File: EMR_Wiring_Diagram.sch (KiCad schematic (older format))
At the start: 22 parts, among them SW1 Switch_DPST, SW2 Switch_DPST

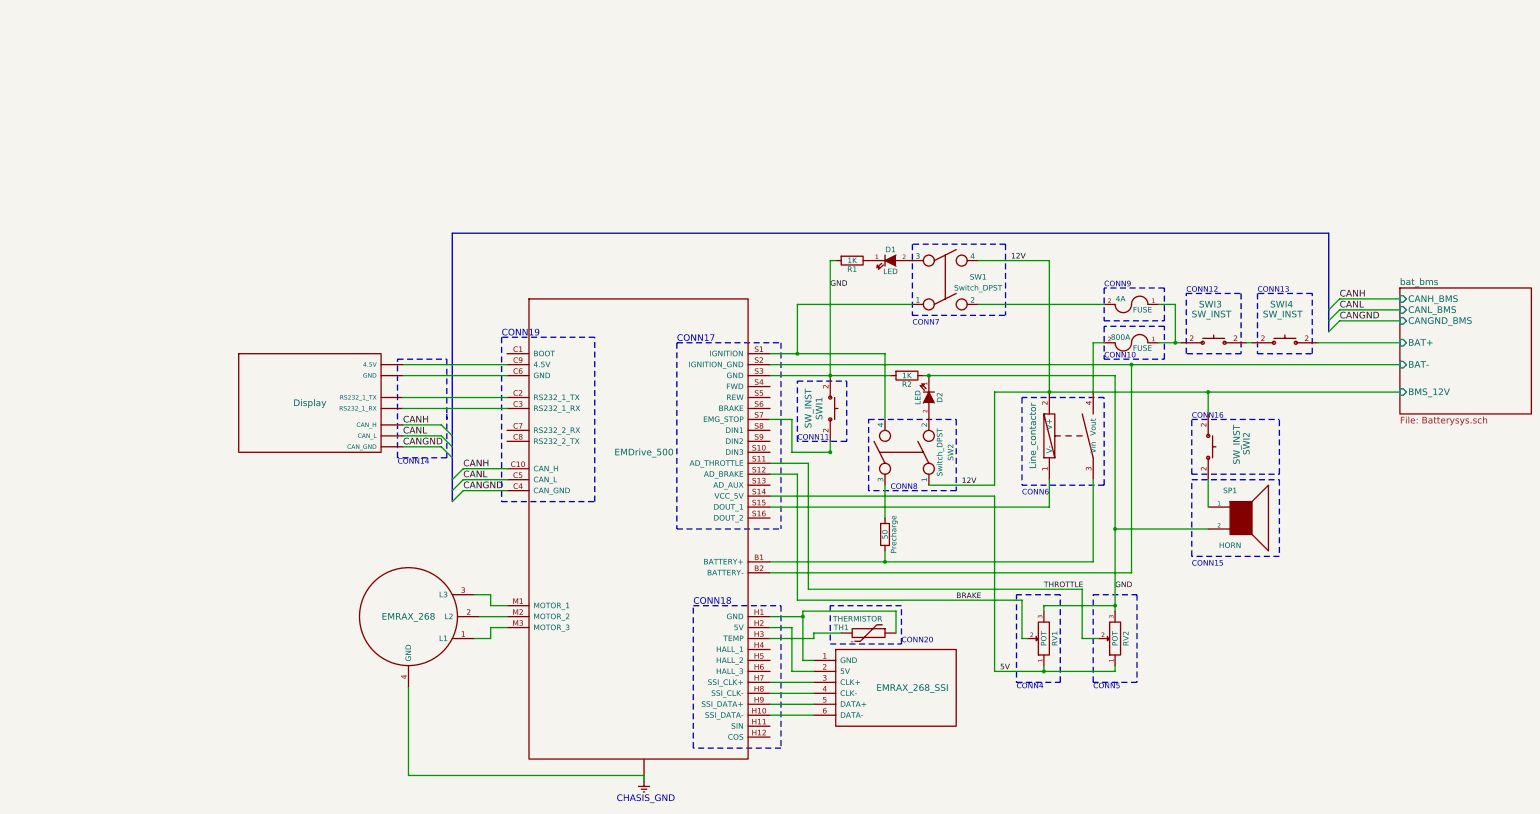
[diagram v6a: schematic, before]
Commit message: Changed a few labels
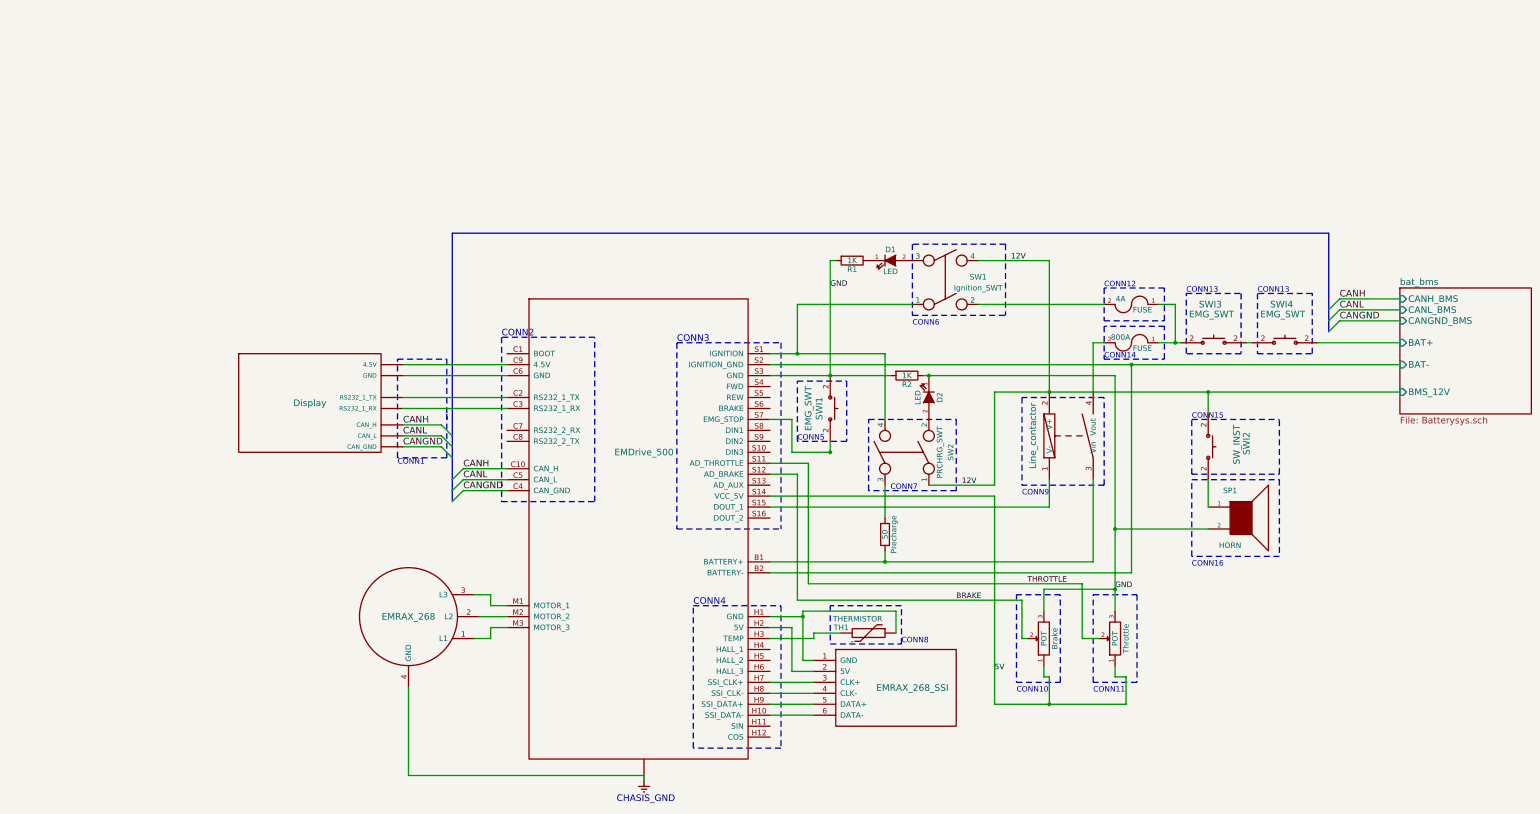
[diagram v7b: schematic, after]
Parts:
- SW1: value Switch_DPST -> Ignition_SWT
- SW2: value Switch_DPST -> PRCHRG_SWT
- SWI1, SWI3, SWI4: value SW_INST -> EMG_SWT
- renumbered RV1 to Brake, RV2 to Throttle
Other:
- note added: "CONN12"
- note added: "CONN13"
- note added: "CONN14\n"
- note added: "CONN15\n"
- note added: "CONN16"
- note added: "CONN1\n\n"
- note added: "CONN2"
- note added: "CONN3"
- note added: "CONN4"
- note added: "CONN5"
- note added: "CONN8"
- note removed: "CONN12\n"
- note removed: "CONN14\n\n"
- note removed: "CONN15"
- note removed: "CONN16\n"
- note removed: "CONN17"
- note removed: "CONN18\n"
- note removed: "CONN19\n"
- note removed: "CONN20\n"
- note removed: "CONN4\n\n"
- note removed: "CONN5\n\n"
- note removed: "CONN8\n"
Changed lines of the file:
@@
 P 9100 3150
 F 0 "SW1" H 9400 3200 50  0000 C CNN
-F 1 "Switch_DPST" H 9400 3100 50  0000 C CNN
+F 1 "Ignition_SWT" H 9400 3100 50  0000 C CNN
 F 2 "" H 9100 3150 50  0000 C CNN
 F 3 "" H 9100 3150 50  0000 C CNN
@@
 $EndComp
 $Comp
-L POT RV2
+L POT Throttle
 U 1 1 56CA241D
 P 10650 6400
-F 0 "RV2" H 10650 6300 50  0000 C CNN
+F 0 "Throttle" H 10650 6300 50  0000 C CNN
 F 1 "POT" H 10650 6400 50  0000 C CNN
 F 2 "" H 10650 6400 50  0000 C CNN
@@
 $EndComp
 $Comp
-L POT RV1
+L POT Brake
 U 1 1 56CA2081
 P 10000 6400
-F 0 "RV1" H 10000 6300 50  0000 C CNN
+F 0 "Brake" H 10000 6300 50  0000 C CNN
 F 1 "POT" H 10000 6400 50  0000 C CNN
 F 2 "" H 10000 6400 50  0000 C CNN
@@
 P 8050 4300
 F 0 "SWI1" H 8050 4200 60  0000 C CNN
-F 1 "SW_INST" H 8050 4100 60  0000 C CNN
+F 1 "EMG_SWT" H 8050 4100 60  0000 C CNN
 F 2 "" H 8030 4560 60  0000 C CNN
 F 3 "" H 8030 4560 60  0000 C CNN
@@
 $EndComp
 Text Notes 5050 3650 0    60   ~ 0
-CONN19\n
+CONN2
 Text Notes 6650 3700 0    60   ~ 0
-CONN17
+CONN3
 Text Notes 6800 6100 0    60   ~ 0
-CONN18\n
+CONN4
 $Comp
 L SW_INST SWI3
@@
 P 11550 3700
 F 0 "SWI3" H 11520 4050 60  0000 C CNN
-F 1 "SW_INST" H 11530 3960 60  0000 C CNN
+F 1 "EMG_SWT" H 11530 3960 60  0000 C CNN
 F 2 "" H 11530 3960 60  0000 C CNN
 F 3 "" H 11530 3960 60  0000 C CNN
@@
 P 12200 3700
 F 0 "SWI4" H 12170 4050 60  0000 C CNN
-F 1 "SW_INST" H 12180 3960 60  0000 C CNN
+F 1 "EMG_SWT" H 12180 3960 60  0000 C CNN
 F 2 "" H 12180 3960 60  0000 C CNN
 F 3 "" H 12180 3960 60  0000 C CNN
@@
 Text Notes 6100 7900 0    60   ~ 0
 CHASIS_GND\n
-Text Notes 9750 6950 0    50   ~ 0
-CONN4\n\n
-Text Notes 10450 6950 0    50   ~ 0
-CONN5\n\n
+Text Notes 9750 6900 0    50   ~ 0
+CONN10\n
+Text Notes 10450 6900 0    50   ~ 0
+CONN11\n
 Text Notes 9800 5100 0    50   ~ 0
+CONN9
+Text Notes 8800 3550 0    50   ~ 0
 CONN6
-Text Notes 8800 3550 0    50   ~ 0
-CONN7
 $Comp
 L Switch_DPST SW2
@@
 P 8750 4700
 F 0 "SW2" H 8750 4300 50  0000 C CNN
-F 1 "Switch_DPST" H 8750 4400 50  0000 C CNN
+F 1 "PRCHRG_SWT" H 8750 4400 50  0000 C CNN
 F 2 "" H 8750 4700 50  0000 C CNN
 F 3 "" H 8750 4700 50  0000 C CNN
@@
 $EndComp
 Text Notes 8600 5050 0    50   ~ 0
-CONN8\n
+CONN7
 Text Notes 10550 3200 0    50   ~ 0
-CONN9
+CONN12
 Text Notes 10550 3850 0    50   ~ 0
-CONN10\n
+CONN14\n
 Text Notes 7750 4600 0    50   ~ 0
-CONN11\n
+CONN5
 Text Notes 11300 3250 0    50   ~ 0
-CONN12\n
+CONN13
 Text Notes 11950 3250 0    50   ~ 0
 CONN13\n
 Text Label 10650 5950 0    50   ~ 0
 GND
-Text Label 10000 5950 0    50   ~ 0
+Text Label 9850 5900 0    50   ~ 0
 THROTTLE
 Text Label 9200 6050 0    50   ~ 0
 BRAKE
-Text Label 9600 6700 0    50   ~ 0
+Text Label 9550 6700 0    50   ~ 0
 5V
 Text Label 8050 3200 0    50   ~ 0
@@
 12V
 Text Notes 4100 4900 0    50   ~ 0
-CONN14\n\n
+CONN1\n\n
 $Comp
 L SPEAKER SP1
@@
 Connection ~ 7800 6200
 Wire Wire Line
-	7850 4800 7850 5950
+	7850 4800 7850 5900
 Wire Wire Line
 	7750 4900 7750 6050
 Wire Wire Line
-	7850 5950 10350 5950
+	7850 5900 10350 5900
 Wire Wire Line
 	7750 6050 9800 6050
 Connection ~ 8950 4000
 Wire Wire Line
-	9550 5100 9550 6700
+	9550 5100 9550 7000
 Wire Wire Line
 	10650 4000 10650 5400
 Wire Wire Line
-	10650 5400 10650 6100
-Wire Wire Line
-	10650 6100 10650 6150
+	10650 5400 10650 5950
+Wire Wire Line
+	10650 5950 10650 6150
 Wire Wire Line
 	7700 4400 7700 4700
@@
 Wire Wire Line
 	11850 3700 11900 3700
-Connection ~ 10650 6100
-Wire Wire Line
-	10000 6100 10000 6150
-Wire Wire Line
-	10650 6100 10000 6100
-Wire Wire Line
-	10350 5950 10350 6400
+Connection ~ 10650 5950
+Wire Wire Line
+	10000 5950 10000 6150
+Wire Wire Line
+	10650 5950 10000 5950
+Wire Wire Line
+	10350 5900 10350 6400
 Wire Wire Line
 	9800 6050 9800 6400
@@
 	10350 6400 10500 6400
 Wire Wire Line
-	10650 6700 10650 6650
-Wire Wire Line
-	10000 6700 10000 6650
-Connection ~ 10000 6700
-Wire Wire Line
-	9550 6700 10000 6700
-Wire Wire Line
-	10000 6700 10650 6700
+	10650 6650 10650 6750
 Wire Notes Line
 	10450 6000 10850 6000
@@
 	11350 5650 11350 4950
 Text Notes 11350 5750 0    50   ~ 0
-CONN15
+CONN16
 Text Notes 11350 4400 0    50   ~ 0
-CONN16\n
+CONN15\n
 Wire Wire Line
 	8650 6150 7800 6150
@@
 	8700 6100 8050 6100
 Text Notes 8700 6450 0    50   ~ 0
-CONN20\n
+CONN8
+Wire Wire Line
+	9550 7000 10050 7000
+Wire Wire Line
+	10050 7000 10750 7000
+Wire Wire Line
+	10750 7000 10750 6750
+Wire Wire Line
+	10750 6750 10650 6750
+Wire Wire Line
+	10000 6650 10000 6750
+Wire Wire Line
+	10000 6750 10050 6750
+Wire Wire Line
+	10050 6750 10050 7000
+Connection ~ 10050 7000
 $EndSCHEMATC

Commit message: Fixed up a few things
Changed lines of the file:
@@
 	1    0    0    -1
 $EndComp
-Text Notes 5050 3650 0    60   ~ 0
+Text Notes 5400 3650 0    60   ~ 0
 CONN2
 Text Notes 6650 3700 0    60   ~ 0
